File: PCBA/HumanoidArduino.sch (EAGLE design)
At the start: 23 parts, among them IC1 7805TV, J2 22-27-2041-04

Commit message: Continued work on PCBA
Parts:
- added JP10, JP11, JP12, JP13, JP14, JP15, JP16, JP17, JP18, JP19, JP20, JP21, JP22, JP23, JP24, JP25: (no value), jumper:JP2E
- added JP9: (no value), jumper:JP1E
- added R7: 670R, SparkFun-Passives:RESISTOR0805-RES
- added R8: 330R, SparkFun-Passives:RESISTOR0805-RES
- added S1: (no value), SparkFun-Electromechanical:SWITCH-SPDTPTH_LOCK
- added U$1: P-CHANNEL-MOSFET, GeekAmmo:P-CHANNEL-MOSFET
- added U$2, U$4: HSMC-C265, SparkFun-Retired:HSMC-C265
- JP1, JP2, JP3, JP4, JP5, JP6, JP7, JP8: device jumper:JP2W -> jumper:JP2E
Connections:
- net 12.6V renamed 12.6V_CHG
- net 4.2V renamed 4.2V_CHG
- new net +5V1: JP10.2, JP11.2, JP12.2, JP13.2, JP14.2, JP15.2, JP16.2, JP17.2, JP18.2, JP19.2, JP20.2, JP21.2, JP22.2, JP23.2, JP24.2, JP25.2
- new net 8.4V_CHG: J2-3.S
- new net 8.4V_IN: JP9.2, S1.P
- new net N$10: JP10.1, R4D.1
- new net N$11: JP11.1, R4C.1
- new net N$12: JP12.1, R4B.1
- new net N$13: JP13.1, R4A.1
- new net N$14: JP14.1, R3D.1
- new net N$15: JP15.1, R3C.1
- new net N$16: JP16.1, R3B.1
- new net N$17: JP17.1, R3A.1
- new net N$18: JP18.1, R2D.1
- new net N$19: JP19.1, R2C.1
- new net N$20: JP20.1, R2B.1
- new net N$21: JP21.1, R2A.1
- new net N$22: JP22.1, R1D.1
- new net N$23: JP23.1, R1C.1
- new net N$24: JP24.1, R1B.1
- new net N$25: JP25.1, R1A.1
- new net N$26: S1.S, U$1.S
- new net N$28: R7.1, U$4.A
- new net N$29: R8.1, U$2.A
- new net N$6: JP5.1, R5D.1
- new net N$7: JP6.1, R5C.1
- new net N$8: JP7.1, R5B.1
- new net N$9: JP8.1, R5A.1
- net +5V: now also R8.2
- net 8.4V: now also R7.2, U$1.D; no longer J2-3.S
- net GND: now also JP10.3, JP11.3, JP12.3, JP13.3, JP14.3, JP15.3, JP16.3, JP17.3, JP18.3, JP19.3, JP20.3, JP21.3, JP22.3, JP23.3, JP24.3, JP25.3, JP9.1, U$1.G, U$2.C, U$4.C
- net N$3: now also JP2.1; no longer JP3.1
- net N$4: now also JP3.1; no longer JP4.1
- net N$5: now also JP4.1; no longer JP5.1
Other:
- moved on the sheet: IC1, J2-1, J2-2, J2-3, J2-4, JP2, JP3, JP4, JP5

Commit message: more PCBA work
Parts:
- added F1, F10, F11, F12, F13, F14, F15, F16, F17, F18, F19, F2, F20, F21, F22, F23, F24, F25, F26, F3, F4, F5, F6, F7, F8, F9: POLYSWITCH, HumanoidLbr:POLYSWITCH
- added JP26, JP27: JUMPER_3X1_0.1, HumanoidLbr:JUMPER_3X1_0.1
- added R10, R9: (no value), SparkFun-Resistors:RESISTOR-ARRAY0603-ARV
- JP1, JP10, JP11, JP12, JP13, JP14, JP15, JP16, JP17, JP18, JP19, JP2, JP20, JP21, JP22, JP23, JP24, JP25, JP3, JP4, JP5, JP6, JP7, JP8: value (none) -> JUMPER_3X1_0.1; device jumper:JP2E -> HumanoidLbr:JUMPER_3X1_0.1
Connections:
- removed net +5V1: JP10.2, JP11.2, JP12.2, JP13.2, JP14.2, JP15.2, JP16.2, JP17.2, JP18.2, JP19.2, JP20.2, JP21.2, JP22.2, JP23.2, JP24.2, JP25.2
- new net N$27: F1.P$1, JP1.2
- new net N$30: F2.P$1, JP2.2
- new net N$31: JP12.1, R4C.1
- new net N$32: JP13.1, R4D.1
- new net N$33: JP14.1, R3A.1
- new net N$34: JP15.1, R3B.1
- new net N$35: JP16.1, R3C.1
- new net N$36: JP17.1, R3D.1
- new net N$38: F21.P$1, JP22.2
- new net N$39: F20.P$1, JP21.2
- new net N$40: F19.P$1, JP20.2
- new net N$41: F18.P$1, JP19.2
- new net N$42: F17.P$1, JP18.2
- new net N$43: JP18.1, R9A.2
- new net N$44: JP19.1, R9B.2
- new net N$45: JP20.1, R9C.2
- new net N$46: JP21.1, R9D.2
- new net N$47: JP22.1, R10A.2
- new net N$48: F22.P$1, JP23.2
- new net N$49: F23.P$1, JP24.2
- new net N$50: F24.P$1, JP25.2
- new net N$51: F25.P$1, JP26.2
- new net N$52: F26.P$1, JP27.2
- new net N$53: JP23.1, R10B.2
- new net N$54: JP24.1, R10C.2
- new net N$55: JP25.1, R10D.2
- net +5V: now also F1.P$2, F10.P$2, F11.P$2, F12.P$2, F13.P$2, F14.P$2, F15.P$2, F16.P$2, F17.P$2, F18.P$2, F19.P$2, F2.P$2, F20.P$2, F21.P$2, F22.P$2, F23.P$2, F24.P$2, F25.P$2, F26.P$2, F3.P$2, F4.P$2, F5.P$2, F6.P$2, F7.P$2, F8.P$2, F9.P$2; no longer JP1.2, JP2.2, JP3.2, JP4.2, JP5.2, JP6.2, JP7.2, JP8.2
- net GND: now also JP26.3, JP27.3; no longer JP10.3, JP11.3, JP12.3, JP13.3, JP14.3, JP15.3, JP16.3, JP17.3, JP5.3, JP6.3, JP7.3, JP8.3
- net N$10: now also F14.P$1, JP15.2; no longer JP10.1, R4D.1
- net N$11: now also F13.P$1, JP14.2; no longer JP11.1, R4C.1
- net N$12: now also F12.P$1, JP13.2; no longer JP12.1, R4B.1
- net N$13: now also F11.P$1, JP12.2; no longer JP13.1, R4A.1
- net N$14: now also F10.P$1, JP11.2; no longer JP14.1, R3D.1
- net N$15: now also F9.P$1, JP10.2; no longer JP15.1, R3C.1
- net N$16: now also F8.P$1, JP8.2; no longer JP16.1, R3B.1
- net N$17: now also F7.P$1, JP7.2; no longer JP17.1, R3A.1
- net N$18: now also F6.P$1, JP6.2; no longer JP18.1, R2D.1
- net N$19: now also F5.P$1, JP5.2; no longer JP19.1, R2C.1
- net N$2: now also R6A.1; no longer R6D.1
- net N$20: now also JP5.1, R5A.1; no longer JP20.1, R2B.1
- net N$21: now also JP6.1, R5B.1; no longer JP21.1, R2A.1
- net N$22: now also JP7.1, R5C.1; no longer JP22.1, R1D.1
- net N$23: now also JP8.1, R5D.1; no longer JP23.1, R1C.1
- net N$24: now also JP10.1, R4A.1; no longer JP24.1, R1B.1
- net N$25: now also JP11.1, R4B.1; no longer JP25.1, R1A.1
- net N$3: now also R6B.1; no longer R6C.1
- net N$4: now also R6C.1; no longer R6B.1
- net N$5: now also R6D.1; no longer R6A.1
- net N$6: now also F3.P$1, JP3.2; no longer JP5.1, R5D.1
- net N$7: now also F4.P$1, JP4.2; no longer JP6.1, R5C.1
- net N$8: now also F16.P$1, JP17.2; no longer JP7.1, R5B.1
- net N$9: now also F15.P$1, JP16.2; no longer JP8.1, R5A.1
- net PWM0: now also R6A.2; no longer R6D.2
- net PWM1: now also R6B.2; no longer R6C.2
- net PWM10: now also R4C.2; no longer R4B.2
- net PWM11: now also R4D.2; no longer R4A.2
- net PWM12: now also R3A.2
- net PWM13: now also R3B.2
- net PWM14: now also R3C.2
- net PWM15: now also R3D.2
- net PWM16: now also R9D.1; no longer R3D.2
- net PWM17: now also R9C.1; no longer R3C.2
- net PWM18: now also R9B.1; no longer R3B.2
- net PWM19: now also R9A.1; no longer R3A.2
- net PWM2: now also R6C.2; no longer R6B.2
- net PWM20: now also R10D.1; no longer R2D.2
- net PWM21: now also R10C.1; no longer R2C.2
- net PWM22: no longer R2B.2
- net PWM23: now also R10A.1; no longer R2A.2
- net PWM24: no longer R1D.2
- net PWM25: no longer R1C.2
- net PWM26: no longer R1B.2
- net PWM27: no longer R1A.2
- net PWM3: now also R6D.2; no longer R6A.2
- net PWM4: now also R5A.2; no longer R5D.2
- net PWM5: now also R5B.2; no longer R5C.2
- net PWM6: now also R5C.2; no longer R5B.2
- net PWM7: now also R5D.2; no longer R5A.2
- net PWM8: now also R4A.2; no longer R4D.2
- net PWM9: now also R4B.2; no longer R4C.2
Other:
- moved on the sheet: H1, H2, H3, R1A, R1B, R1C, R1D, R2A, R2B, R2C, R2D, R3A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

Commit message: Working on PCB
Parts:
- added C1: 100nF, capacitor-wima:C2,5-3
- added C2, C3: 22p, capacitor-wima:C2,5-3
- added Q1: 12MHz, crystal:CSM-7X-DU
- added U4: CH340G, HumanoidLbr:CH340G
- added X1: MINI-USB-UX60-MB-5S8, con-hirose:MINI-USB-UX60-MB-5S8
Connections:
- new net D+: U4.D+, X1.3
- new net D-: U4.D-, X1.2
- new net N$56: C2.1, Q1.2, U4.XI
- new net N$57: C3.1, Q1.1, U4.XO
- new net RX: U$3.UART-TX, U4.RXD
- new net TX: U$3.UART-RX, U4.TXD
- net +5V: now also C1.1, U4.VCC, X1.1
- net GND: now also C1.2, C2.2, C3.2, U4.GND, X1.5
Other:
- note added: "BATTERY CHG"
- note added: "BATTERY PWR"
- note removed: "BATTERY"
- moved on the sheet: IC1, J2-1, J2-2, J2-3, J2-4, R7, R8, U$2, U$3, U$4

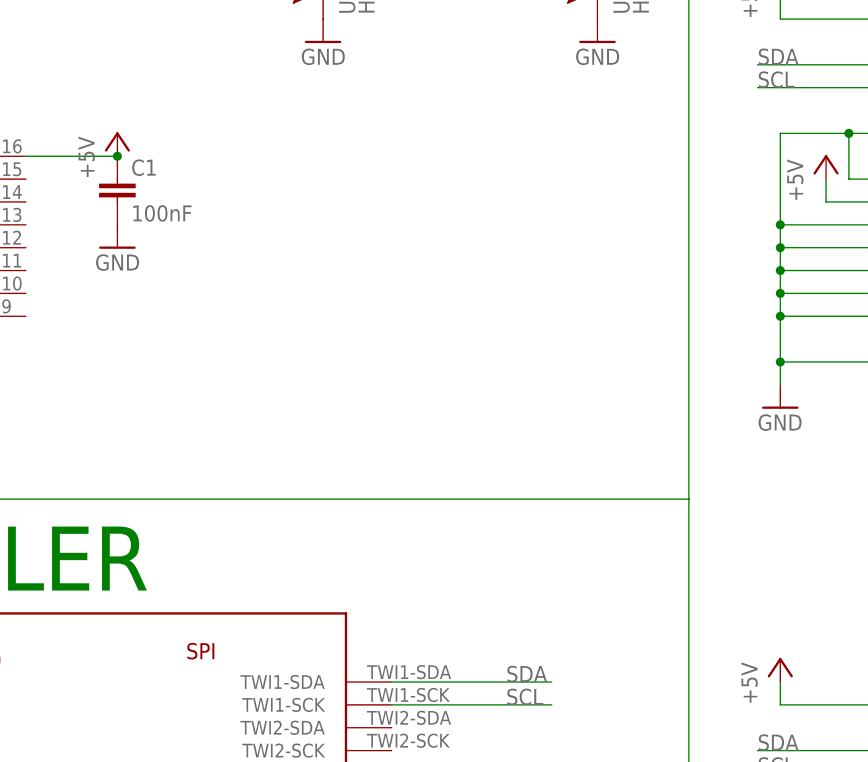
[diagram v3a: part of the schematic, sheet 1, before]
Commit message: Added boost circuit for charging
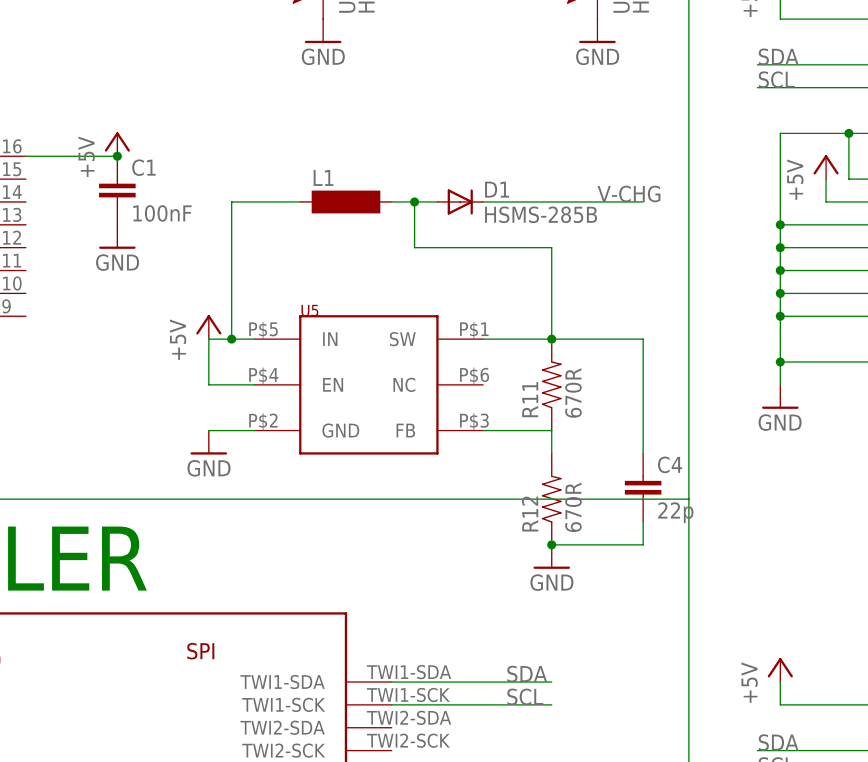
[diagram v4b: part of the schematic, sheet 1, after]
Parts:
- added C4: 22p, capacitor-wima:C2,5-3
- added D1: HSMS-285B, avago:HSMS-285B
- added L1: (no value), inductor-neosid:SM-1206
- added R11, R12: 670R, SparkFun-Passives:RESISTOR0805-RES
- added U5: SX1308_B628, HumanoidLbr:SX1308_B628
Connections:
- new net N$58: L1.1, U5.EN, U5.IN
- new net N$59: R12.2, U5.FB
- new net N$60: C4.1, D1.A, L1.2, R11.2, U5.SW
- new net V-CHG: D1.C
- net GND: now also C4.2, R12.1, U5.GND
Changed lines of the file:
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@@
 <part name="GND38" library="supply1" deviceset="GND" device=""/>
 <part name="Q1" library="crystal" deviceset="CSM-7X-DU" device="" value="12MHz"/>
+<part name="U5" library="HumanoidLbr" deviceset="SX1308_B628" device=""/>
+<part name="P+11" library="supply1" deviceset="+5V" device=""/>
+<part name="GND39" library="supply1" deviceset="GND" device=""/>
+<part name="R11" library="SparkFun-Passives" deviceset="RESISTOR" device="0805-RES" value="670R"/>
+<part name="R12" library="SparkFun-Passives" deviceset="RESISTOR" device="0805-RES" value="670R"/>
+<part name="GND40" library="supply1" deviceset="GND" device=""/>
+<part name="C4" library="capacitor-wima" deviceset="C" device="2,5-3" value="22p"/>
+<part name="D1" library="avago" deviceset="HSMS-285B" device=""/>
+<part name="L1" library="inductor-neosid" deviceset="SM-1206" device=""/>
 </parts>
 <sheets>
@@
 <instance part="GND38" gate="1" x="40.64" y="180.34" rot="MR90"/>
 <instance part="Q1" gate="P" x="53.34" y="180.34" rot="R90"/>
+<instance part="U5" gate="G$1" x="134.62" y="172.72"/>
+<instance part="P+11" gate="1" x="116.84" y="180.34"/>
+<instance part="GND39" gate="1" x="116.84" y="165.1" rot="MR0"/>
+<instance part="R11" gate="G$1" x="154.94" y="172.72" rot="R90"/>
+<instance part="R12" gate="G$1" x="154.94" y="160.02" rot="R90"/>
+<instance part="GND40" gate="1" x="154.94" y="152.4" rot="MR0"/>
+<instance part="C4" gate="G$1" x="165.1" y="162.56"/>
+<instance part="D1" gate="A" x="144.78" y="193.04"/>
+<instance part="L1" gate="G$1" x="132.08" y="193.04"/>
 </instances>
 <busses>
@@
 <junction x="43.18" y="180.34"/>
 <wire x1="43.18" y1="180.34" x2="43.18" y2="185.42" width="0.1524" layer="91"/>
+</segment>
+<segment>
+<pinref part="U5" gate="G$1" pin="GND"/>
+<pinref part="GND39" gate="1" pin="GND"/>
+<wire x1="121.92" y1="167.64" x2="116.84" y2="167.64" width="0.1524" layer="91"/>
+</segment>
+<segment>
+<pinref part="R12" gate="G$1" pin="1"/>
+<pinref part="GND40" gate="1" pin="GND"/>
+<pinref part="C4" gate="G$1" pin="2"/>
+<wire x1="165.1" y1="157.48" x2="165.1" y2="154.94" width="0.1524" layer="91"/>
+<wire x1="165.1" y1="154.94" x2="154.94" y2="154.94" width="0.1524" layer="91"/>
+<junction x="154.94" y="154.94"/>
 </segment>
 </net>
@@
 </segment>
 </net>
+<net name="N$58" class="0">
+<segment>
+<pinref part="U5" gate="G$1" pin="IN"/>
+<wire x1="121.92" y1="177.8" x2="119.38" y2="177.8" width="0.1524" layer="91"/>
+<wire x1="119.38" y1="177.8" x2="116.84" y2="177.8" width="0.1524" layer="91"/>
+<wire x1="116.84" y1="177.8" x2="116.84" y2="172.72" width="0.1524" layer="91"/>
+<pinref part="U5" gate="G$1" pin="EN"/>
+<wire x1="116.84" y1="172.72" x2="121.92" y2="172.72" width="0.1524" layer="91"/>
+<pinref part="L1" gate="G$1" pin="1"/>
+<wire x1="119.38" y1="177.8" x2="119.38" y2="193.04" width="0.1524" layer="91"/>
+<wire x1="119.38" y1="193.04" x2="127" y2="193.04" width="0.1524" layer="91"/>
+<junction x="119.38" y="177.8"/>
+</segment>
+</net>
+<net name="N$59" class="0">
+<segment>
+<pinref part="U5" gate="G$1" pin="FB"/>
+<pinref part="R12" gate="G$1" pin="2"/>
+<wire x1="147.32" y1="167.64" x2="154.94" y2="167.64" width="0.1524" layer="91"/>
+<wire x1="154.94" y1="167.64" x2="154.94" y2="165.1" width="0.1524" layer="91"/>
+</segment>
+</net>
+<net name="N$60" class="0">
+<segment>
+<pinref part="U5" gate="G$1" pin="SW"/>
+<pinref part="R11" gate="G$1" pin="2"/>
+<wire x1="147.32" y1="177.8" x2="154.94" y2="177.8" width="0.1524" layer="91"/>
+<pinref part="C4" gate="G$1" pin="1"/>
+<wire x1="154.94" y1="177.8" x2="165.1" y2="177.8" width="0.1524" layer="91"/>
+<wire x1="165.1" y1="177.8" x2="165.1" y2="165.1" width="0.1524" layer="91"/>
+<junction x="154.94" y="177.8"/>
+<wire x1="154.94" y1="177.8" x2="154.94" y2="187.96" width="0.1524" layer="91"/>
+<wire x1="154.94" y1="187.96" x2="139.7" y2="187.96" width="0.1524" layer="91"/>
+<pinref part="L1" gate="G$1" pin="2"/>
+<pinref part="D1" gate="A" pin="A"/>
+<wire x1="137.16" y1="193.04" x2="139.7" y2="193.04" width="0.1524" layer="91"/>
+<wire x1="139.7" y1="193.04" x2="142.24" y2="193.04" width="0.1524" layer="91"/>
+<wire x1="139.7" y1="187.96" x2="139.7" y2="193.04" width="0.1524" layer="91"/>
+<junction x="139.7" y="193.04"/>
+</segment>
+</net>
+<net name="V-CHG" class="0">
+<segment>
+<pinref part="D1" gate="A" pin="C"/>
+<wire x1="147.32" y1="193.04" x2="165.1" y2="193.04" width="0.1524" layer="91"/>
+<label x="160.02" y="193.04" size="1.778" layer="95"/>
+</segment>
+</net>
